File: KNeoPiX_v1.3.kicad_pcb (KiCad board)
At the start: 4 copper layers, 24.5 x 34.6 mm, 32 parts, among them J1 Conn_KNX, J2 Conn_KNX, J3 Screw Terminal - Non Isolated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, J4 Screw Terminal - Isolated IOs, J5 Conn_01x05, SW1 Prog BTN, U1 Seeeduino XIAO, U2 LM2937IMP-3.3 / 5.0, U3 ADuM1201AR / ADum1250, U4 ADum1250

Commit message: Pre-Ready for  1st Prod. Needs to be checked again.
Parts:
- removed REF**: LOGO, KNeoPix:OpenKNX_Logo_07x05
- added J6: Conn_01x05, Connector_PinHeader_1.00mm:PinHeader_1x05_P1.00mm_Vertical, F.Cu at (129.7, 122.5)
- added REF1: LOGO, KNeoPix:OpenKNX_Logo_05x03, B.Cu at (117.2, 125.8)
- added REF2: LOGO, KNeoPix:OpenKNX_Logo_07x05, B.Cu at (126.2, 109.3)
- J5: footprint Connector_PinHeader_1.27mm:PinHeader_1x05_P1.27mm_Vertical -> Connector_JST:JST_SH_BM05B-SRSS-TB_1x05-1MP_P1.00mm_Vertical
- moved J5 2.94 mm to (131.6, 122.3), turned to 0 degrees
- moved JP1 0.58 mm to (126.4, 118.8), turned to 0 degrees
- moved JP2 0.58 mm to (130.4, 118.8)
- moved JP3 0.58 mm to (134.3, 118.8)
- moved SW1 0.48 mm to (134.6, 114.7)
- moved C7 0.47 mm to (130.2, 114.6)
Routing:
- net RESET: track 15.0 -> 25.4 mm
- net KNX_GND: track 50.0 -> 55.0 mm
- net EXT_VCC_IN: track 64.0 -> 67.4 mm
- net S_3V3: track 96.6 -> 94.2 mm
- net KNX+: track 16.7 -> 14.7 mm
- net EXT_VCC_OUT: track 39.1 -> 37.1 mm
- net D0: track 12.3 -> 10.3 mm
- net EXT_GND: track 110.5 -> 109.0 mm, vias 3 -> 6
- net SWDIO: track 13.2 -> 14.7 mm, vias 0 -> 1
- net SWCLK: track 18.5 -> 19.6 mm
- net NEO_DATA0_OUT: track 30.8 -> 29.9 mm
- net KNX_RX: track 18.8 -> 18.1 mm
- net D6_TX: track 22.1 -> 22.8 mm
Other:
- board text removed: "3V3"
- board text removed: "5V"
- board text removed: "D1"
- board text removed: "D10"
- board text removed: "D2"
- board text removed: "D3"
- board text removed: "D8"
- board text removed: "D9"
- board text removed: "KNX"
- board text removed: "RX"
- board text removed: "SAVE"
- board text removed: "TX"

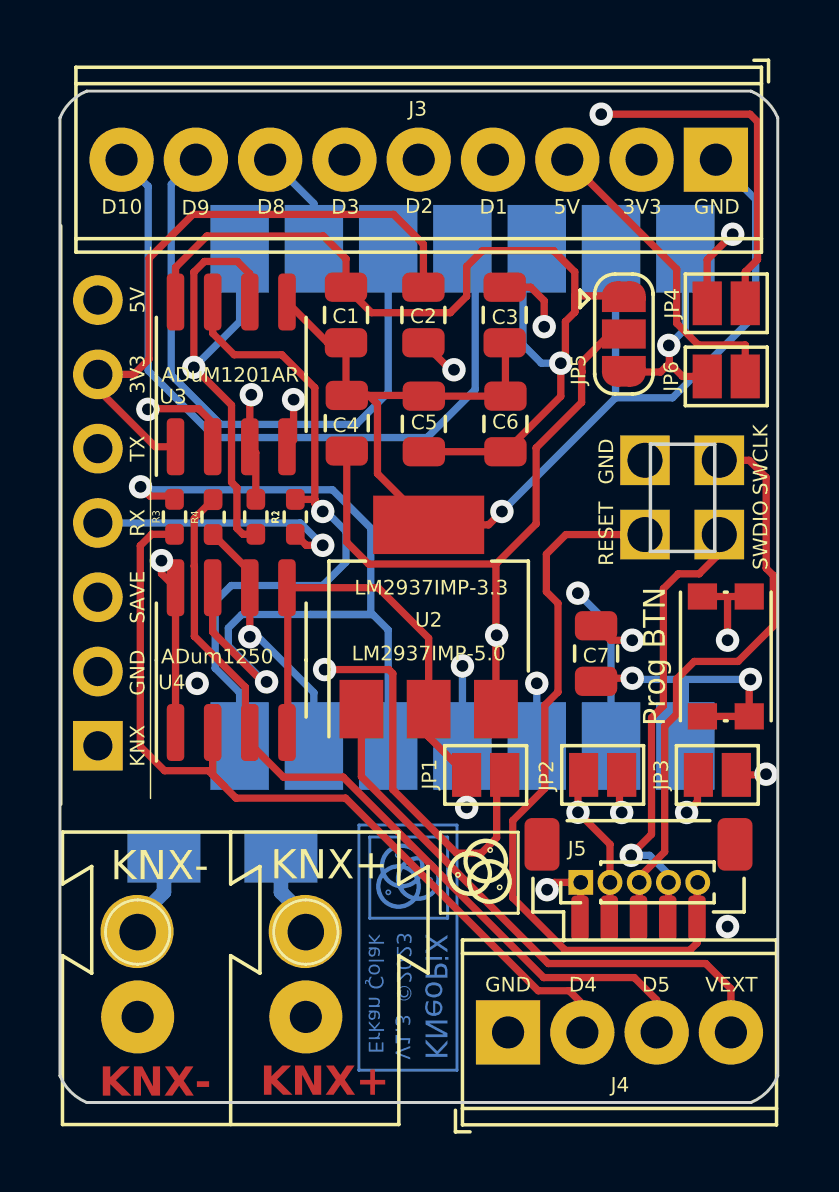
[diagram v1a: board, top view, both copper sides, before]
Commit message: Finalized version v1.3!
Every is now checked and Ready for 1st pcb production!
Next todo is to clean up the whole project, files, folders, footprint and also the 3d files.
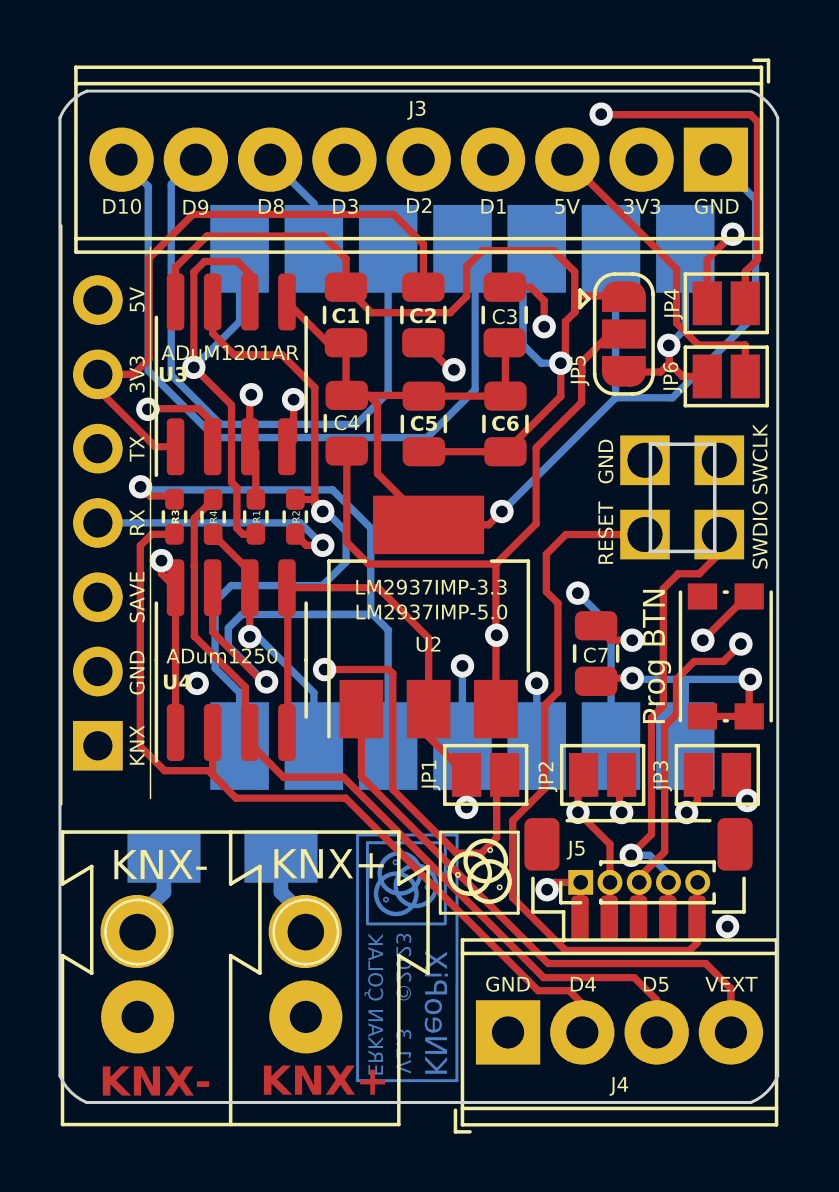
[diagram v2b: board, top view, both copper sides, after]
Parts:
- added REF**: KNeoPix - Logo, KNeoPix-Logo:KNeoPix - Logo, B.Cu at (123.9, 125.2)
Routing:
- net EXT_GND: track 109.0 -> 107.1 mm
- net SWCLK: track 19.6 -> 18.7 mm, vias 0 -> 1
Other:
- board text removed: "Erkan Çolak"
- board text removed: "KNeoPiX"
- board text removed: "V1.3"
- board text removed: "©2023"

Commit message: New footprint, folder structure
More cleaned UP!
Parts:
- J5: footprint Connector_JST:JST_SH_BM05B-SRSS-TB_1x05-1MP_P1.00mm_Vertical -> KNeoPix:JST_SH_BM05B-SRSS-TB_1x05-1MP_P1.00mm_Vertical
- J6: footprint Connector_PinHeader_1.00mm:PinHeader_1x05_P1.00mm_Vertical -> KNeoPix:PinHeader_1x05_P1.00mm_Vertical
- REF42: renamed from REF**; footprint KNeoPix-Logo:KNeoPix - Logo -> KNeoPix:KNeoPix - Logo
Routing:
- net EXT_GND: track 107.1 -> 110.2 mm
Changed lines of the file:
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@@
     )
   )
-  (footprint "Connector_JST:JST_SH_BM05B-SRSS-TB_1x05-1MP_P1.00mm_Vertical" (layer "F.Cu")
+  (footprint "KNeoPix:JST_SH_BM05B-SRSS-TB_1x05-1MP_P1.00mm_Vertical" (layer "F.Cu")
     (at 131.625 122.35)
     (descr "JST SH series connector, BM05B-SRSS-TB (http://www.jst-mfg.com/product/pdf/eng/eSH.pdf), generated with kicad-footprint-generator")
@@
     )
   )
-  (footprint "Connector_PinHeader_1.00mm:PinHeader_1x05_P1.00mm_Vertical" (layer "F.Cu")
+  (footprint "KNeoPix:PinHeader_1x05_P1.00mm_Vertical" (layer "F.Cu")
     (at 129.65 122.45 90)
     (descr "Through hole straight pin header, 1x05, 1.00mm pitch, single row")
@@
     )
   )
-  (footprint "KNeoPix-Logo:KNeoPix - Logo" (layer "B.Cu")
+  (footprint "KNeoPix:KNeoPix - Logo" (layer "B.Cu")
     (at 123.94 125.17 90)
-    (fp_text reference "REF**" (at 0.05 6.75 270 unlocked) (layer "B.SilkS") hide
+    (attr board_only exclude_from_bom allow_soldermask_bridges)
+    (fp_text reference "REF42" (at 0.05 6.75 270 unlocked) (layer "B.SilkS") hide
         (effects (font (size 1 1) (thickness 0.15)) (justify mirror))
     )
@@
   (segment (start 125.75 119.887416) (end 125.75 118.775) (width 0.25) (layer "F.Cu") (net 19))
   (segment (start 124.45 117.475) (end 125.75 118.775) (width 0.25) (layer "F.Cu") (net 19))
+  (segment (start 133.81 112.675) (end 133.81 114.1555) (width 0.25) (layer "F.Cu") (net 19))
   (segment (start 135.3205 112.675) (end 135.41 112.675) (width 0.25) (layer "F.Cu") (net 19))
   (segment (start 121.625 104) (end 121.625 105.775) (width 0.25) (layer "F.Cu") (net 19))
@@
   (segment (start 129.65 122.45) (end 129.65 123.65) (width 0.25) (layer "F.Cu") (net 19))
   (segment (start 128.7495 122.45) (end 128.5 122.6995) (width 0.25) (layer "F.Cu") (net 19))
+  (segment (start 133.81 114.1555) (end 133.825 114.1705) (width 0.25) (layer "F.Cu") (net 19))
   (segment (start 119.605 102.605) (end 121 104) (width 0.25) (layer "F.Cu") (net 19))
   (segment (start 133.825 114.1705) (end 135.3205 112.675) (width 0.25) (layer "F.Cu") (net 19))
@@
   (segment (start 121.65 105.8) (end 122.4 105.8) (width 0.25) (layer "F.Cu") (net 19))
   (segment (start 127.075 105.825) (end 127.075 104.025) (width 0.25) (layer "F.Cu") (net 19))
+  (segment (start 133.81 112.675) (end 135.41 112.675) (width 0.25) (layer "F.Cu") (net 19))
   (via (at 134.67 123.96) (size 0.8) (drill 0.4) (layers "F.Cu" "B.Cu") (net 19))
   (via (at 128.5 122.6995) (size 0.8) (drill 0.4) (layers "F.Cu" "B.Cu") (net 19))
